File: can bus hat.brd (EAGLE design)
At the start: 52.5 x 65 mm, 47 parts, among them J1 RASPBERRYPI-40-PIN-GPIO_PTH_N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, Q1 16MHz, U2 ESP32-WROVER, U4 MCP2515, U5 MCP2551, U6 HEX_CONVERTER, X1 DB9 Plug

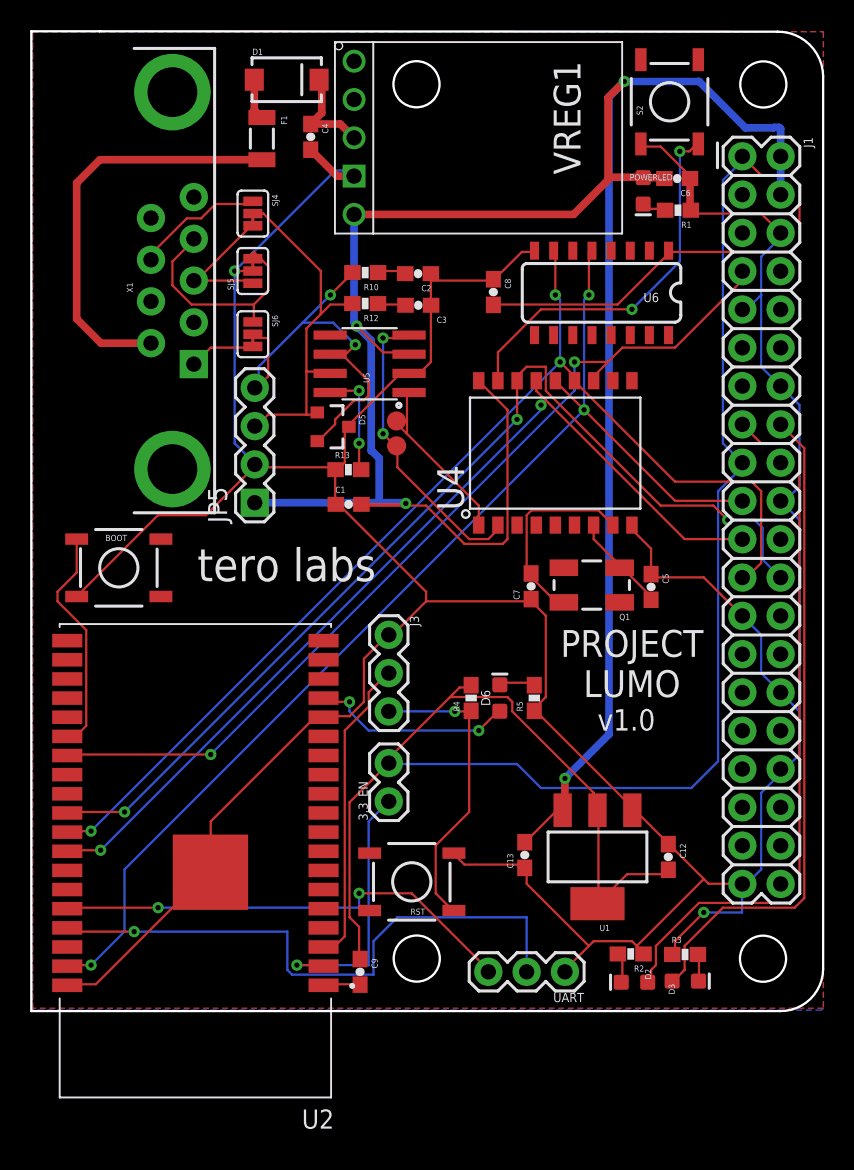
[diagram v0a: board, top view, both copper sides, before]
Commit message: Updated SILK
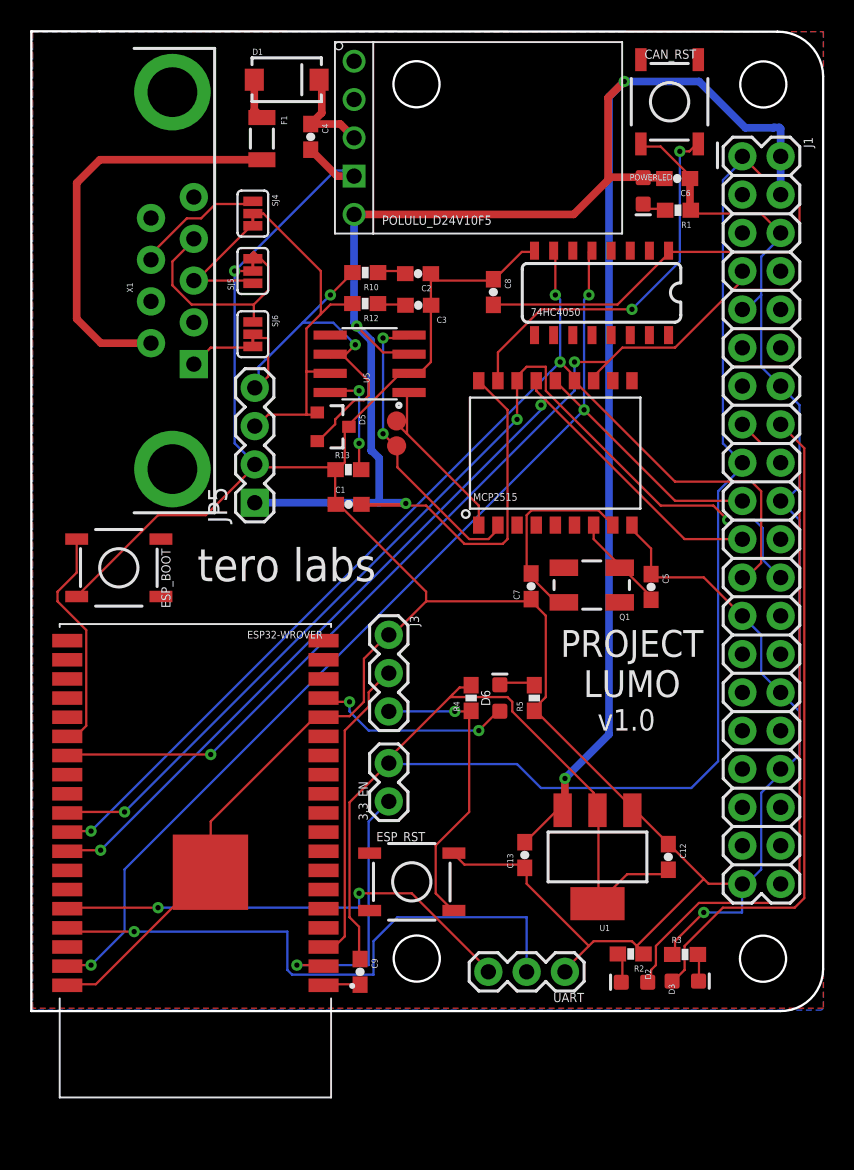
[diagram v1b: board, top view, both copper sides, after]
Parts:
- renumbered BOOT to ESP_BOOT, RST to ESP_RST, S2 to CAN_RST, U2 to ESP32-WROVER, U6 to 74HC4050, VREG1 to POLULU_D24V10F5
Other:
- board text added: "MCP2515"

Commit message: updated bom, fixed cap values
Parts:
- C12, C13: value 0.1uF -> 10uF
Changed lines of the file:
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@@
 <drawing>
 <settings>
-<setting alwaysvectorfont="yes"/>
+<setting alwaysvectorfont="no"/>
 <setting verticaltext="up"/>
 </settings>
 <grid distance="50" unitdist="mil" unit="mil" style="lines" multiple="1" display="yes" altdistance="5" altunitdist="mil" altunit="mil"/>
 <layers>
-<layer number="1" name="Top" color="4" fill="1" visible="no" active="yes"/>
+<layer number="1" name="Top" color="4" fill="1" visible="yes" active="yes"/>
 <layer number="2" name="Route2" color="16" fill="1" visible="no" active="no"/>
 <layer number="3" name="Route3" color="17" fill="1" visible="no" active="no"/>
@@
 <layer number="27" name="tValues" color="7" fill="1" visible="no" active="yes"/>
 <layer number="28" name="bValues" color="7" fill="1" visible="no" active="yes"/>
-<layer number="29" name="tStop" color="7" fill="3" visible="no" active="yes"/>
+<layer number="29" name="tStop" color="7" fill="3" visible="yes" active="yes"/>
 <layer number="30" name="bStop" color="7" fill="6" visible="no" active="yes"/>
 <layer number="31" name="tCream" color="7" fill="4" visible="no" active="yes"/>
@@
 <attribute name="VALUE" x="133.223" y="8.636" size="0.6096" layer="27" font="vector" ratio="20" rot="R90"/>
 </element>
-<element name="C12" library="SparkFun-Capacitors" package="0603-CAP" value="0.1uF" x="149.733" y="6.223" smashed="yes" rot="R270">
+<element name="C12" library="SparkFun-Capacitors" package="0603-CAP" value="10uF" x="149.733" y="6.223" smashed="yes" rot="R270">
 <attribute name="NAME" x="150.495" y="7.112" size="0.4064" layer="25" font="vector" rot="R270"/>
 <attribute name="PROD_ID" value="CAP-00810" x="149.733" y="6.223" size="1.778" layer="27" rot="R270" display="off"/>
 <attribute name="VALUE" x="148.59" y="7.239" size="0.4064" layer="27" font="vector" rot="R270"/>
 </element>
-<element name="C13" library="SparkFun-Capacitors" package="0603-CAP" value="0.1uF" x="140.208" y="6.35" smashed="yes" rot="R90">
+<element name="C13" library="SparkFun-Capacitors" package="0603-CAP" value="10uF" x="140.208" y="6.35" smashed="yes" rot="R90">
 <attribute name="NAME" x="139.446" y="5.461" size="0.4064" layer="25" font="vector" rot="R90"/>
 <attribute name="PROD_ID" value="CAP-00810" x="140.208" y="6.35" size="1.778" layer="27" rot="R90" display="off"/>
